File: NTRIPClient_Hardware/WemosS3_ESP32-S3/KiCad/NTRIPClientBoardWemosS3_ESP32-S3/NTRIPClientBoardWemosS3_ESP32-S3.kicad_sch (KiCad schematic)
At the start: 4 parts, among them U1 Wemos_S3_ESP32-S3

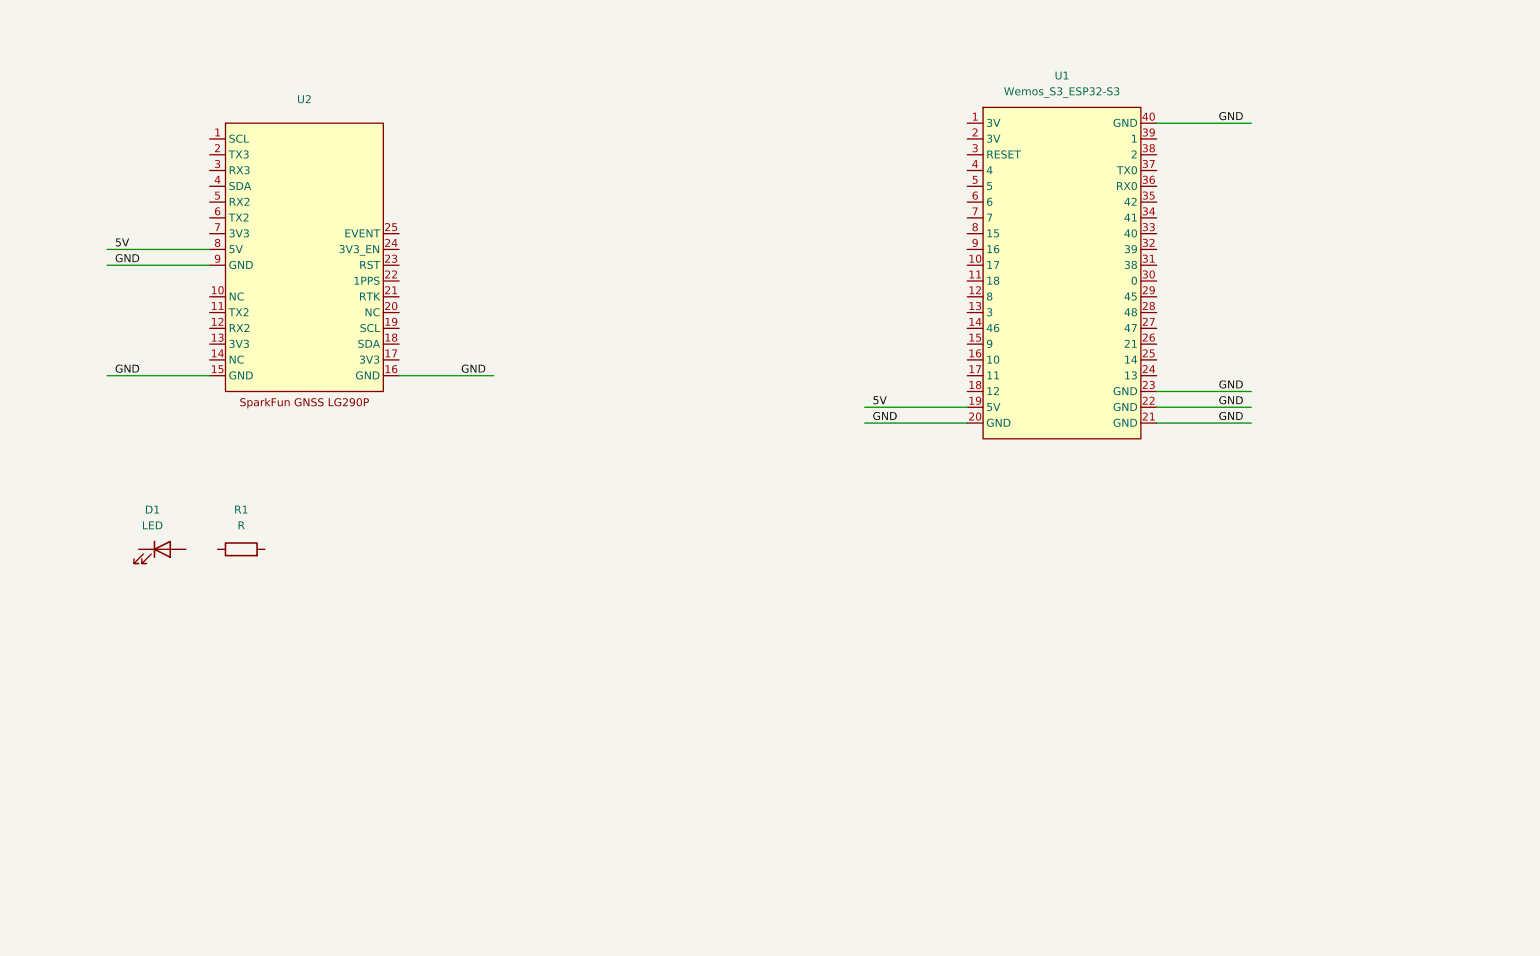
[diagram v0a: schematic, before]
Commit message: Updated PCB for LOLIN S3 WEMOS board to version 1.0
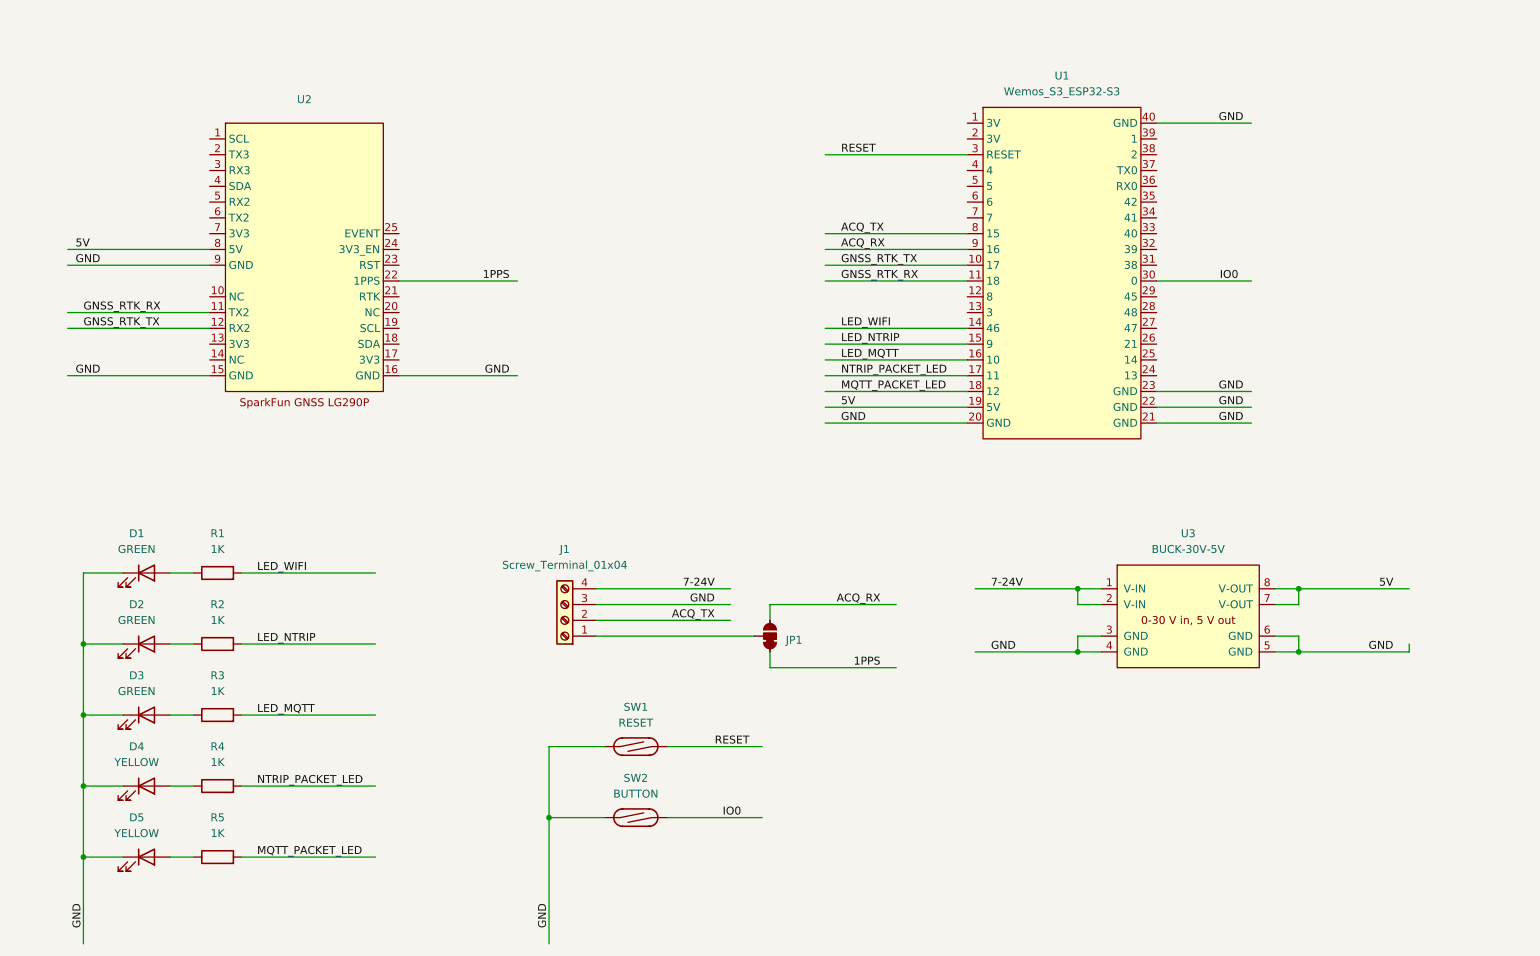
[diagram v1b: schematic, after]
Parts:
- added D2, D3: GREEN, LED_SMD:LED_1206_3216Metric, symbol Device:LED
- added D4, D5: YELLOW, LED_SMD:LED_1206_3216Metric, symbol Device:LED
- added J1: Screw_Terminal_01x04, Connector_Phoenix_MSTB:PhoenixContact_MSTBVA_2,5_4-G_1x04_P5.00mm_Vertical, symbol Connector:Screw_Terminal_01x04
- added JP1: ~, SparkFun-Jumper:Jumper_3_NC-1_Trace, symbol SparkFun-Jumper:SolderJumper_3_Bridged12
- added R2, R3, R4, R5: 1K, Resistor_SMD:R_1206_3216Metric, symbol Device:R
- added SW1: RESET, my-KiCad-library:SW_SPST_REED_20mm, symbol Switch:SW_Reed
- added SW2: BUTTON, my-KiCad-library:SW_SPST_REED_20mm, symbol Switch:SW_Reed
- added U3: BUCK-30V-5V, my-KiCad-library:BUCK-30V-5V, symbol my-KiCad-library:BUCK-30V-5V-ESP32_node
- D1: value LED -> GREEN; footprint (none) -> LED_SMD:LED_1206_3216Metric
- R1: value R -> 1K; footprint (none) -> Resistor_SMD:R_1206_3216Metric
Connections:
- net 5V: now also U3.7 (V-OUT), U3.8 (V-OUT)
- net GND: now also D1.1 (K), D2.1 (K), D3.1 (K), D4.1 (K), D5.1 (K), J1.3 (Pin_3), SW1.1, SW2.1, U3.3 (GND), U3.4 (GND), U3.5 (GND), U3.6 (GND)
- net GNSS_RTK_TX: now reaches U1.10 (17)
- net GNSS_RTK_TX: now also U2.12 (RX2)
- net GNSS_RTK_RX: now reaches U1.11 (18)
- net GNSS_RTK_RX: now also U2.11 (TX2)
- net LED_WIFI: now reaches U1.14 (46)
- net LED_WIFI: now also R1.2
- net LED_NTRIP: now reaches U1.15 (9)
- net LED_NTRIP: now also R2.2
- net LED_MQTT: now reaches U1.16 (10)
- net LED_MQTT: now also R3.2
- net NTRIP_PACKET_LED: now reaches U1.17 (11)
- net NTRIP_PACKET_LED: now also R4.2
- net MQTT_PACKET_LED: now reaches U1.18 (12)
- net MQTT_PACKET_LED: now also R5.2
- net RESET: now reaches U1.3 (RESET)
- net RESET: now also SW1.2
- net IO0: now reaches U1.30 (0)
- net IO0: now also SW2.2
- net ACQ_TX: now reaches U1.8 (15)
- net ACQ_TX: now also J1.2 (Pin_2)
- net ACQ_RX: now reaches U1.9 (16)
- net ACQ_RX: now also JP1.3 (C)
- net at R1.1: now also D1.2 (A)
- net 1PPS: now reaches U2.22 (1PPS)
- net 1PPS: now also JP1.1 (A)
- new net: D2.2 (A), R2.1
- new net: J1.1 (Pin_1), JP1.2 (B)
- new net: D5.2 (A), R5.1
- new net: D4.2 (A), R4.1
- new net: D3.2 (A), R3.1
- new net 7-24V: J1.4 (Pin_4), U3.1 (V-IN), U3.2 (V-IN)
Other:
- moved on the sheet: D1, R1

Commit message: corrected request of mount points so they will be provided when using credentials to the caster Added Atom-Lite M5 to PCB design
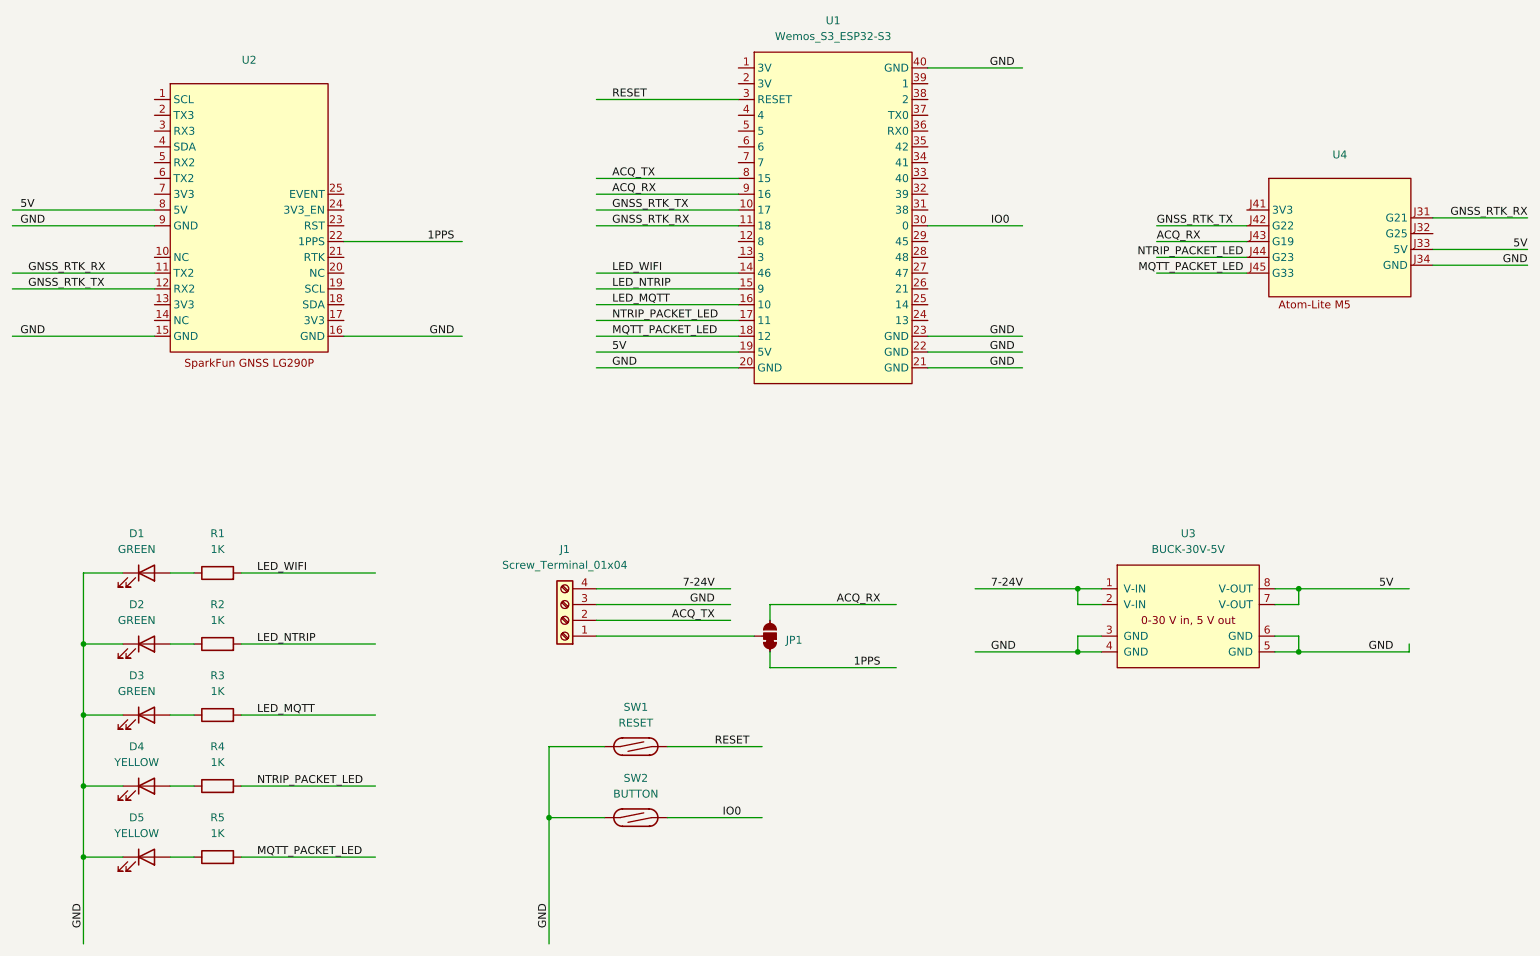
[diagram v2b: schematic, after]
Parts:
- added U4: ~, my-KiCad-library:Atom-Lite_M5, symbol my-KiCad-library:Atom-Lite_M5
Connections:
- net 5V: now also U4.J33 (5V)
- net ACQ_RX: now also U4.J43 (G19)
- net GND: now also U4.J34 (GND)
- net GNSS_RTK_RX: now also U4.J31 (G21)
- net GNSS_RTK_TX: now also U4.J42 (G22)
- net MQTT_PACKET_LED: now also U4.J45 (G33)
- net NTRIP_PACKET_LED: now also U4.J44 (G23)
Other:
- moved on the sheet: U1, U2
